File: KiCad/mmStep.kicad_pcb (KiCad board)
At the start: 2 copper layers, 81 x 49 mm, 39 parts, among them J1 Conn_02x08_Top_Bottom, J10 Screw_Terminal_01x04, J11 Screw_Terminal_01x02, J2 DX07S016JA1R1500, J3 MICROMOD-2222-C, J4 DEBUG, J5 I2C, J6 Screw_Terminal_01x02, J7 Screw_Terminal_01x04, J8 Screw_Terminal_01x04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

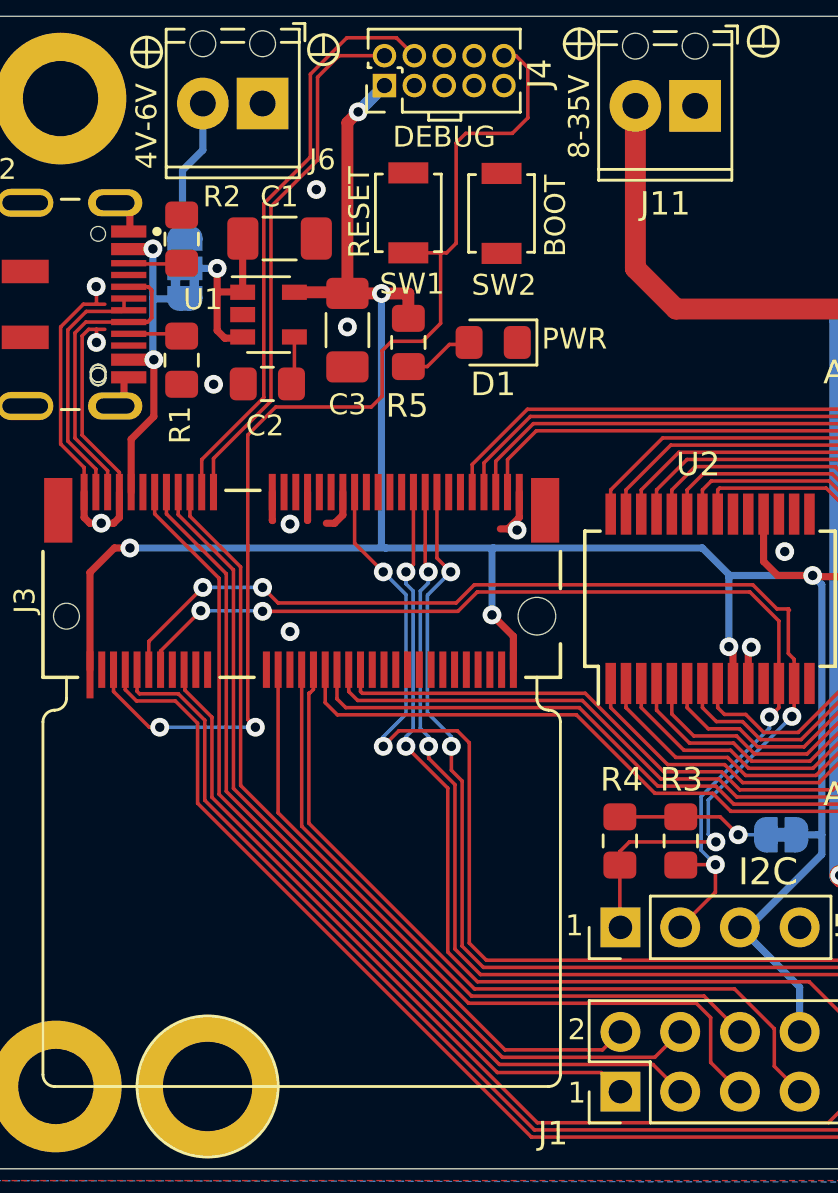
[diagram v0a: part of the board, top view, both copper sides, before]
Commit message: Fixed missing BOOT signal and some ERC errors
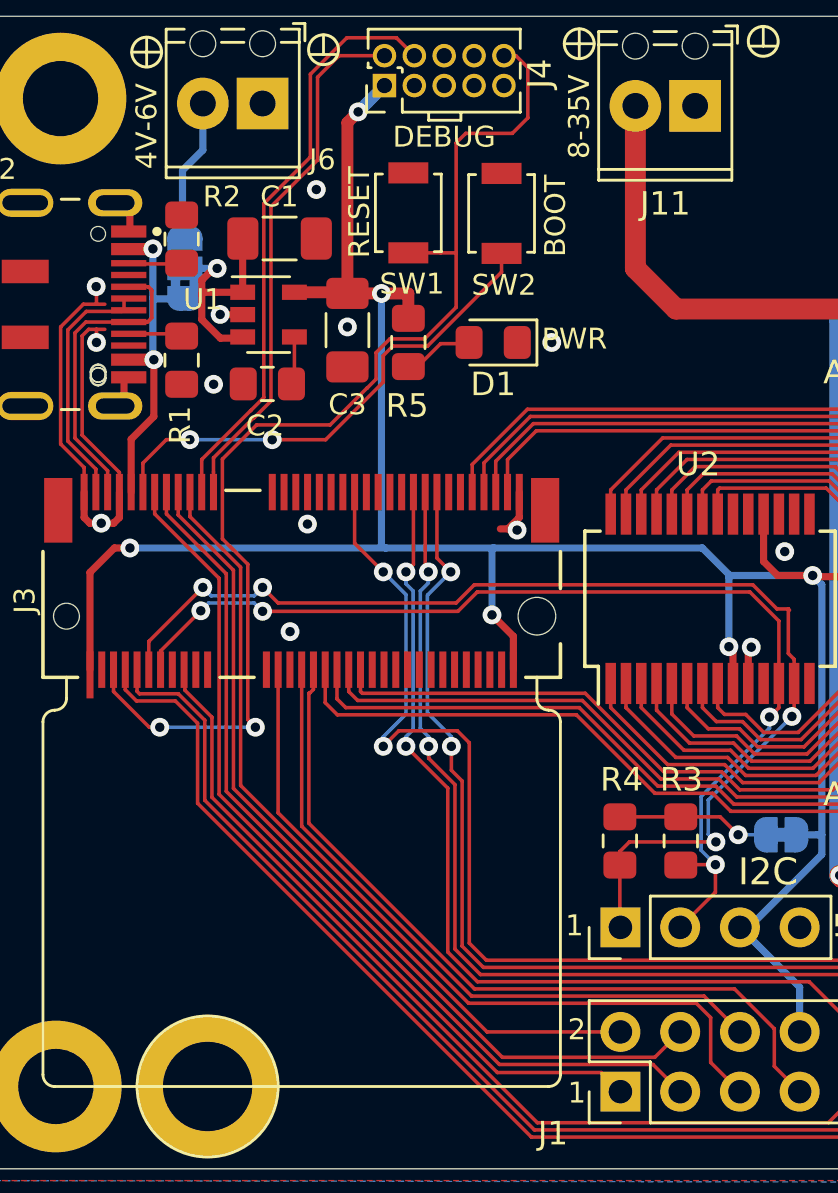
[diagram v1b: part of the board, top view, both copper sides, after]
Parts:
- removed G***: LOGO, prj:logo
- C4, C5, C6, C7: value CP_Small -> 47u
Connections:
- A1 pad 10: /Drivers/M02 -> /Drivers/M01
- A1 pad 11: /Drivers/M12 -> /Drivers/M11
- A1 pad 12: /Drivers/M22 -> /Drivers/M21
- A1 pad 9: /Drivers/~EN2 -> /Drivers/~EN1
- A2 pad 10: /Drivers/M01 -> /Drivers/M02
- A2 pad 11: /Drivers/M11 -> /Drivers/M12
- A2 pad 12: /Drivers/M21 -> /Drivers/M22
- A2 pad 9: /Drivers/~EN1 -> /Drivers/~EN2
- J3 pad 11: (no net) -> BOOT
- SW2 pad 1: (no net) -> BOOT
- U1 pad 2: (no net) -> GND
- U2 pad 1: /Drivers/~EN1 -> /Drivers/~EN2
- U2 pad 2: /Drivers/M01 -> /Drivers/M02
- U2 pad 3: /Drivers/M11 -> /Drivers/M12
- U2 pad 4: /Drivers/M21 -> /Drivers/M22
- U2 pad 5: /Drivers/~EN2 -> /Drivers/~EN1
- U2 pad 6: /Drivers/M02 -> /Drivers/M01
- U2 pad 7: /Drivers/M12 -> /Drivers/M11
- U2 pad 8: /Drivers/M22 -> /Drivers/M21
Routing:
- net /Drivers/M22: track 21.4 -> 46.6 mm
- net /Drivers/M21: track 46.6 -> 21.4 mm
- net /Drivers/M02: track 28.3 -> 53.5 mm
- net /Drivers/M01: track 53.5 -> 28.3 mm
- net /Drivers/M12: track 24.8 -> 50.0 mm
- net /Drivers/M11: track 50.0 -> 24.8 mm
- net /Drivers/~EN2: track 31.9 -> 56.9 mm
- net /Drivers/~EN1: track 56.9 -> 31.9 mm
- net BOOT: track 0.00 -> 21.5 mm, vias 0 -> 2
- net GND: track 34.0 -> 30.7 mm, vias 11 -> 13
- net /V_R: track 8.54 -> 9.89 mm
- net RESET: track 47.1 -> 48.1 mm
- net RX1: track 34.5 -> 33.9 mm
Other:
- rule pad_to_mask_clearance: 0.05 -> 0
- board text added: "select V_IN USB/Terminal STD: USB"

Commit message: cleanup
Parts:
- added G***: LOGO, prj:logo, B.Cu at (30.5, 16.5)
- D1: value LED_Small -> LED_0805
- J10: value Screw_Terminal_01x04 -> Screw Term 100mil 1x4
- J11, J6: value Screw_Terminal_01x02 -> Screw_Term 100mil 1x2
- J3: footprint MicroMod:TE_Connectivity-2199230-4-MFG -> MicroMod:TE_Connectivity-2199230-4-Handsolder
- J4: value DEBUG -> Pin Head 50mil
- J8: value Screw_Terminal_01x04 -> Screw_Term 100mil 1x4
- SW1: value SW_Push -> B3U1000P
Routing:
- net /Drivers/DIR2: track 30.8 -> 31.9 mm
- net RESET: track 48.1 -> 47.2 mm
- net GND: track 30.7 -> 30.8 mm, vias 13 -> 14
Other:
- board text added: "SWD-DEBUG"
- board text removed: "DEBUG"
